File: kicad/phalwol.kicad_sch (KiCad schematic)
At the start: 82 parts, among them J1 AudioJack4, SW1 SW_Push, SW10 SW_Push, SW11 SW_Push, SW12 SW_Push, SW13 SW_Push, SW14 SW_Push, SW15 SW_Push, SW16 SW_Push, SW17 SW_Push, SW18 SW_Push, SW19 SW_Push, SW2 SW_Push, SW20 SW_Push, SW21 SW_Push, SW22 SW_Push, SW23 SW_Push, SW24 SW_Push, SW25 SW_Push, SW26 SW_Push, SW27 SW_Push, SW28 SW_Push, SW29 SW_Push, SW3 SW_Push, SW30 SW_Push, SW31 SW_Push, SW32 SW_Push, SW33 SW_Push, SW34 SW_Push, SW35 SW_Push, SW36 SW_Push, SW37 SW_Push, SW38 SW_Push, SW39 SW_Push, SW4 SW_Push, SW5 SW_Push, SW6 SW_Push, SW7 SW_Push, SW8 SW_Push, SW9 SW_Push, U1 ProMicro

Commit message: update pcb and schema
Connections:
- net VCC: now reaches J1.R1
- net VCC: now also JP1.2 (B), U1.21 (VCC)
- net GND: now reaches J1.R2
- net GND: now also J1.S, JP2.2 (B), U1.23 (GND), U1.3 (GND), U1.4 (GND)
- net SERIAL: now reaches J1.T
- net SERIAL: now also U1.2 (RX1/D2)
- net ROW3: now reaches U1.10 (7/E6)
- net ROW2: now reaches U1.11 (8/B4)
- net ROW1: now reaches U1.12 (9/B5)
- net COL1: now reaches U1.13 (B6/10)
- net COL2: now reaches U1.14 (B2/16)
- net COL3: now reaches U1.15 (B3/14)
- net COL4: now reaches U1.16 (B1/15)
- net COL5: now reaches U1.17 (F7/A0)
- net COL6: now reaches U1.18 (F6/A1)
- net COL7: now reaches U1.19 (F5/A2)
- net COL8: now reaches U1.20 (F4/A3)
- net RST: now reaches U1.22 (RST)
- net HAND: now reaches U1.7 (4/D4)
- net HAND: now also JP1.1 (A), JP2.1 (A)
- net ROW5: now reaches U1.8 (5/C6)
- net ROW4: now reaches U1.9 (6/D7)
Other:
- moved on the sheet: D1, D10, D11, D12, D13, D14, D15, D16, D17, D18, D19, D2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

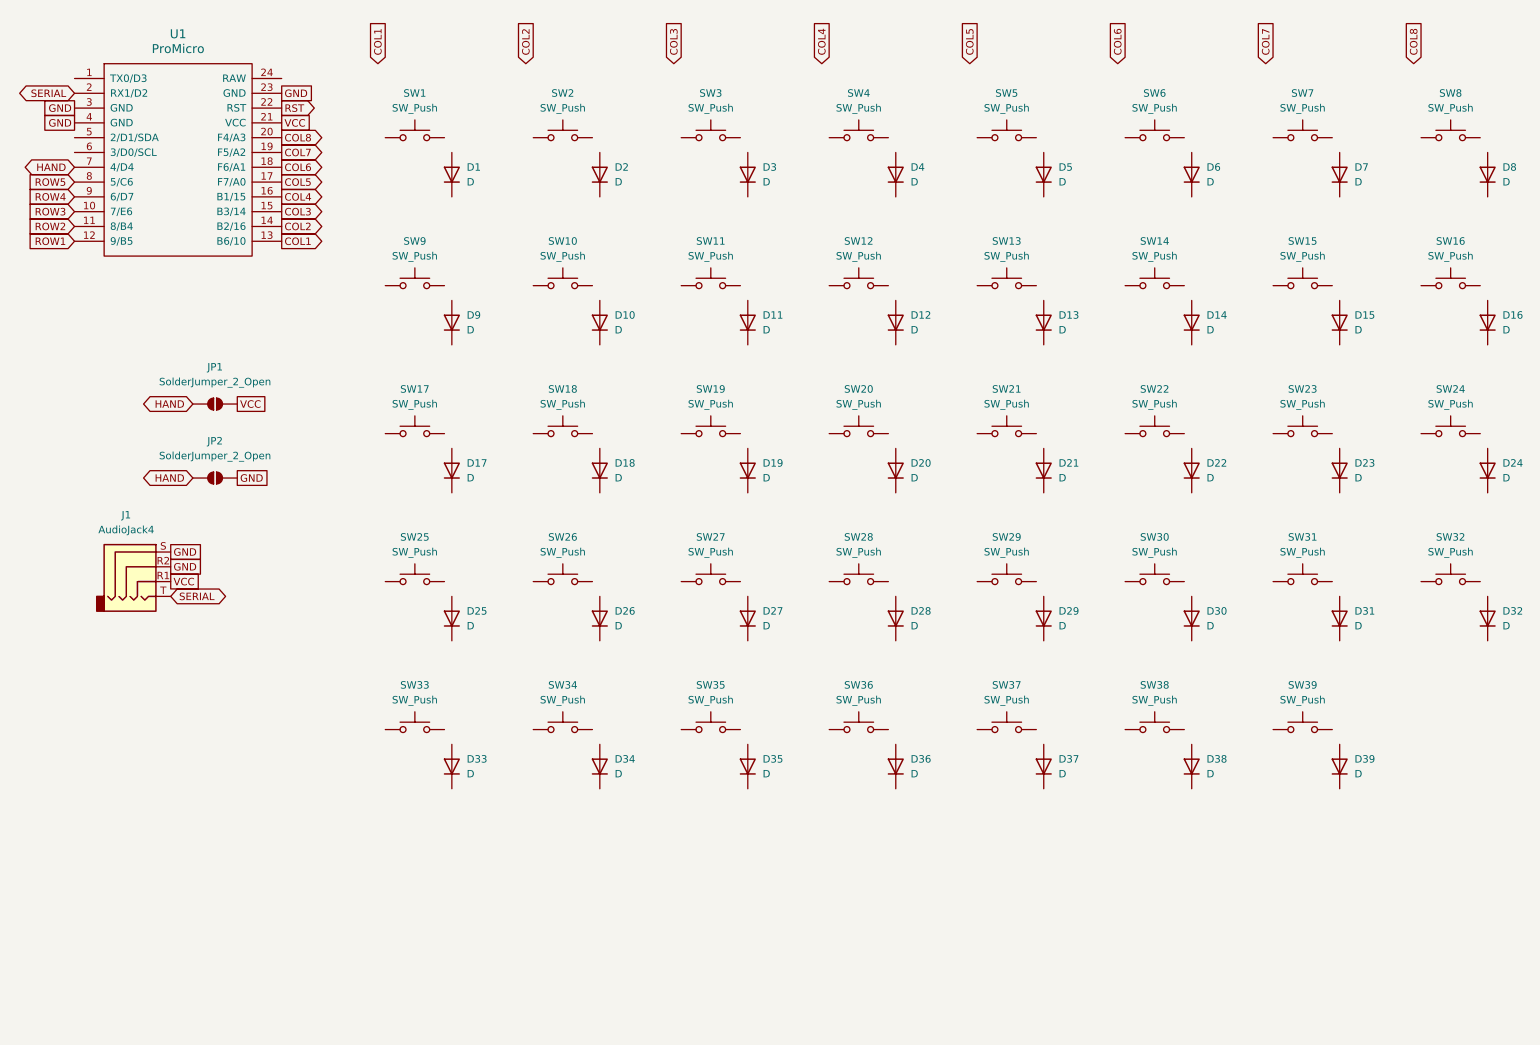
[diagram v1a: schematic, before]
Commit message: connect schema and pcb
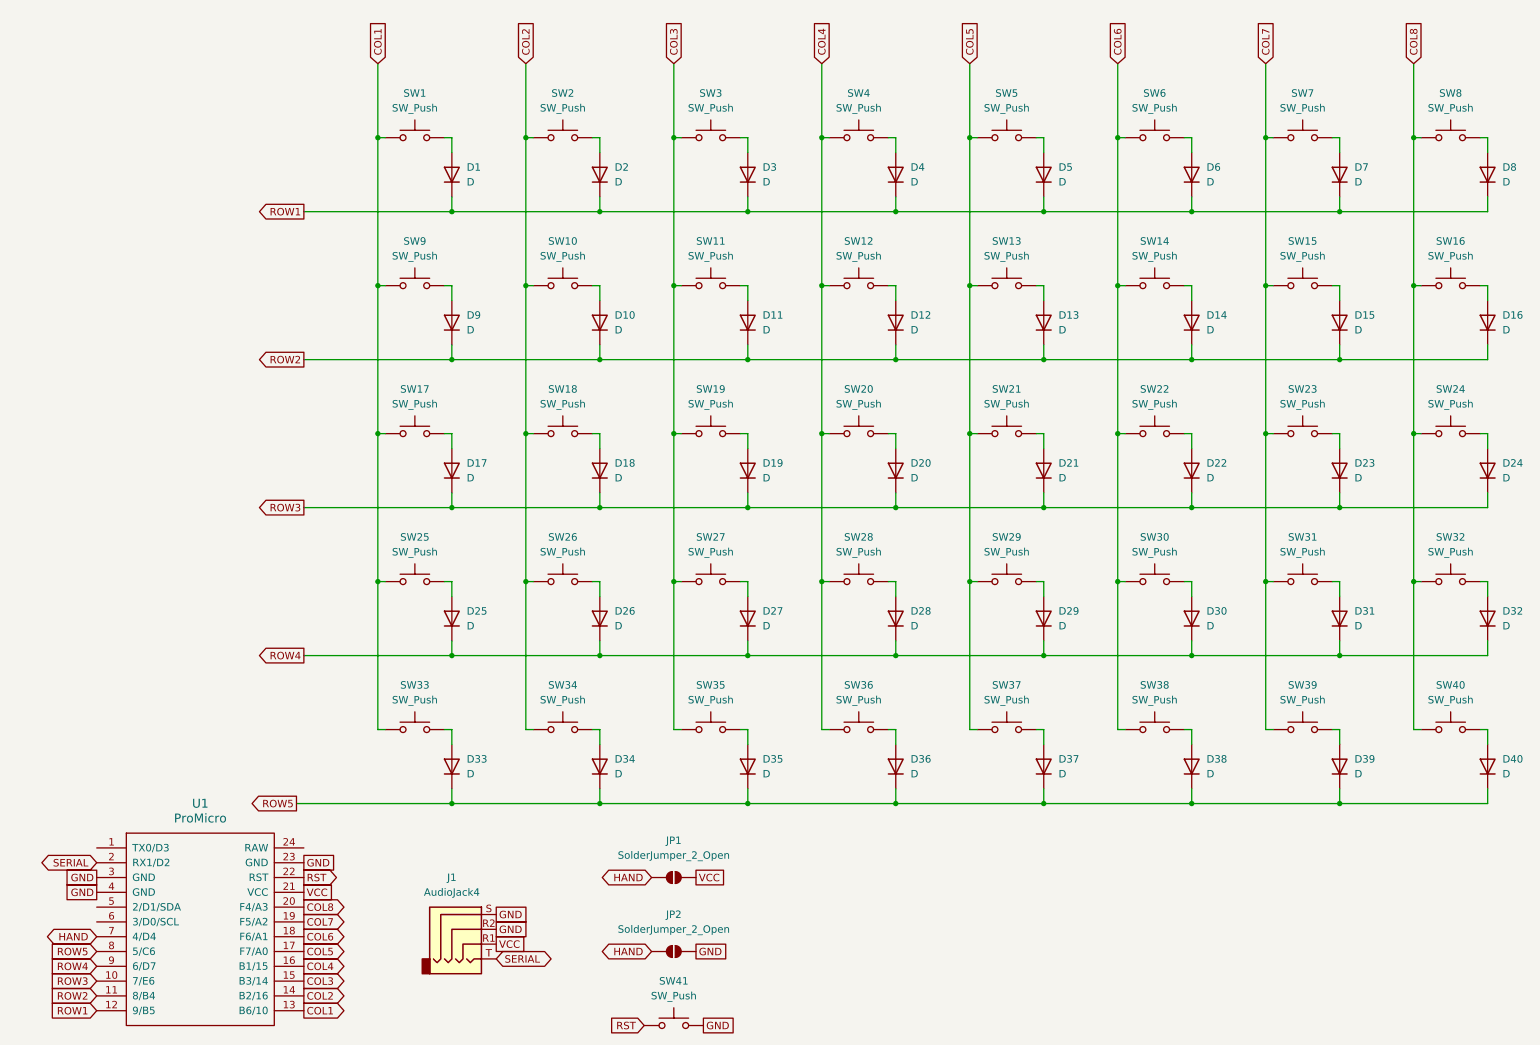
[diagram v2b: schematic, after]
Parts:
- added D40: D, symbol Device:D
- added SW40, SW41: SW_Push, symbol Switch:SW_Push
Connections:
- net COL1: now also SW1.1, SW17.1, SW25.1, SW33.1, SW9.1
- net COL2: now also SW10.1, SW18.1, SW2.1, SW26.1, SW34.1
- net COL3: now also SW11.1, SW19.1, SW27.1, SW3.1, SW35.1
- net COL4: now also SW12.1, SW20.1, SW28.1, SW36.1, SW4.1
- net COL5: now also SW13.1, SW21.1, SW29.1, SW37.1, SW5.1
- net COL6: now also SW14.1, SW22.1, SW30.1, SW38.1, SW6.1
- net COL7: now also SW15.1, SW23.1, SW31.1, SW39.1, SW7.1
- net COL8: now also SW16.1, SW24.1, SW32.1, SW8.1, SW40.1
- net GND: now also SW41.2
- net ROW1: now also D1.1 (K), D2.1 (K), D3.1 (K), D4.1 (K), D5.1 (K), D6.1 (K), D7.1 (K), D8.1 (K)
- net ROW2: now also D10.1 (K), D11.1 (K), D12.1 (K), D13.1 (K), D14.1 (K), D15.1 (K), D16.1 (K), D9.1 (K)
- net ROW3: now also D17.1 (K), D18.1 (K), D19.1 (K), D20.1 (K), D21.1 (K), D22.1 (K), D23.1 (K), D24.1 (K)
- net ROW4: now also D25.1 (K), D26.1 (K), D27.1 (K), D28.1 (K), D29.1 (K), D30.1 (K), D31.1 (K), D32.1 (K)
- net ROW5: now also D33.1 (K), D34.1 (K), D35.1 (K), D36.1 (K), D37.1 (K), D38.1 (K), D39.1 (K), D40.1 (K)
- net RST: now also SW41.1
- net at D20.2 (A): now also SW20.2
- net at SW31.2: now also D31.2 (A)
- net at D10.2 (A): now also SW10.2
- net at SW17.2: now also D17.2 (A)
- net at D12.2 (A): now also SW12.2
- net at SW19.2: now also D19.2 (A)
- net at D9.2 (A): now also SW9.2
- net at SW26.2: now also D26.2 (A)
- net at D1.2 (A): now also SW1.2
- net at D37.2 (A): now also SW37.2
- net at D13.2 (A): now also SW13.2
- net at D6.2 (A): now also SW6.2
- net at SW2.2: now also D2.2 (A)
- net at SW36.2: now also D36.2 (A)
- net at SW38.2: now also D38.2 (A)
- net at SW32.2: now also D32.2 (A)
- net at SW16.2: now also D16.2 (A)
- net at SW4.2: now also D4.2 (A)
- net at D29.2 (A): now also SW29.2
- net at D22.2 (A): now also SW22.2
- net at SW33.2: now also D33.2 (A)
- net at SW7.2: now also D7.2 (A)
- net at SW35.2: now also D35.2 (A)
- net at D23.2 (A): now also SW23.2
- net at D8.2 (A): now also SW8.2
- net at SW15.2: now also D15.2 (A)
- net at D28.2 (A): now also SW28.2
- net at D24.2 (A): now also SW24.2
- net at SW11.2: now also D11.2 (A)
- net at SW5.2: now also D5.2 (A)
- net at SW14.2: now also D14.2 (A)
- net at D39.2 (A): now also SW39.2
- net at D30.2 (A): now also SW30.2
- net at SW27.2: now also D27.2 (A)
- net at D18.2 (A): now also SW18.2
- net at D3.2 (A): now also SW3.2
- net at SW25.2: now also D25.2 (A)
- net at SW34.2: now also D34.2 (A)
- net at D21.2 (A): now also SW21.2
- new net: D40.2 (A), SW40.2
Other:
- moved on the sheet: J1, JP1, JP2, U1

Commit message: hotfix wiring
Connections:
- net COL1: now also U1.20 (F4/A3); no longer U1.13 (B6/10)
- net COL2: now also U1.19 (F5/A2); no longer U1.14 (B2/16)
- net COL3: now also U1.18 (F6/A1); no longer U1.15 (B3/14)
- net COL4: now also U1.17 (F7/A0); no longer U1.16 (B1/15)
- net COL5: now also U1.16 (B1/15); no longer U1.17 (F7/A0)
- net COL6: now also U1.15 (B3/14); no longer U1.18 (F6/A1)
- net COL7: now also U1.14 (B2/16); no longer U1.19 (F5/A2)
- net COL8: now also U1.13 (B6/10); no longer U1.20 (F4/A3)
- net ROW1: now also U1.8 (5/C6); no longer U1.12 (9/B5)
- net ROW2: now also U1.9 (6/D7); no longer U1.11 (8/B4)
- net ROW4: now also U1.11 (8/B4); no longer U1.9 (6/D7)
- net ROW5: now also U1.12 (9/B5); no longer U1.8 (5/C6)
